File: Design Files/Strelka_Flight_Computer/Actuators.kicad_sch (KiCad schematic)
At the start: 10 parts, among them J3 DB125-3.5-4P-GN-S, J4 SM06B-GHS-TB(LF)(SN)

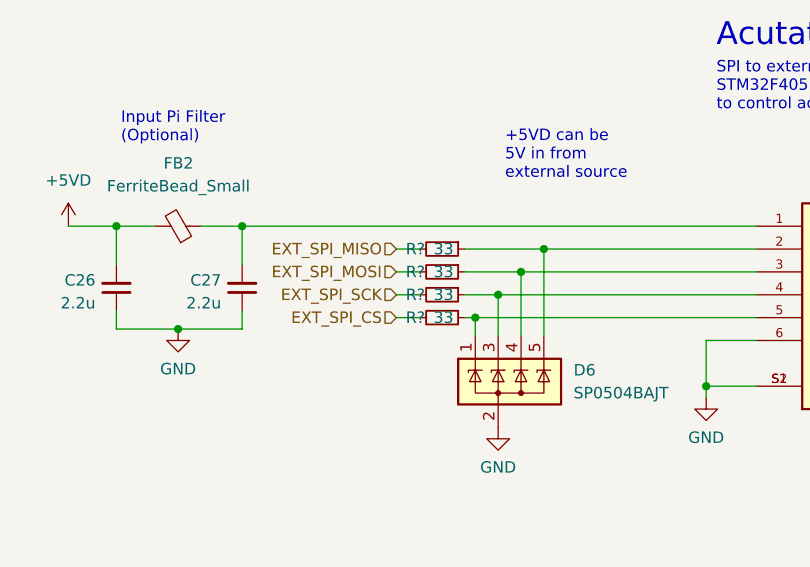
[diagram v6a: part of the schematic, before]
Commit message: Changed boost converter
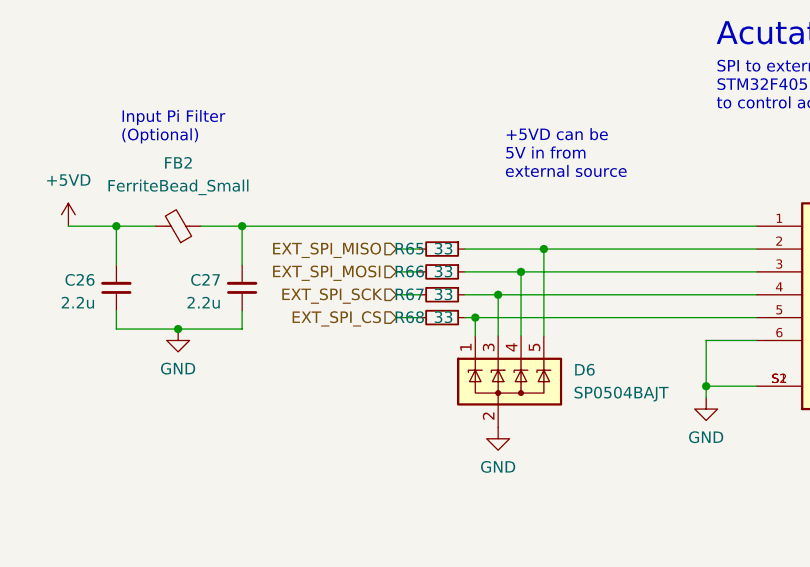
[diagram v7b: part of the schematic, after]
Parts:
- gave numbers to parts that had none: 4
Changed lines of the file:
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@@
   (symbol (lib_id "Device:R_Small") (at 191.135 90.17 270) (unit 1)
     (in_bom yes) (on_board yes)
-    (property "Reference" "R?" (id 0) (at 189.23 90.17 90)
+    (property "Reference" "R66" (id 0) (at 189.23 90.17 90)
       (effects (font (size 1.27 1.27)) (justify right))
     )
@@
   (symbol (lib_id "Device:R_Small") (at 191.135 95.25 270) (unit 1)
     (in_bom yes) (on_board yes)
-    (property "Reference" "R?" (id 0) (at 189.23 95.25 90)
+    (property "Reference" "R68" (id 0) (at 189.23 95.25 90)
       (effects (font (size 1.27 1.27)) (justify right))
     )
@@
   (symbol (lib_id "Device:R_Small") (at 191.135 92.71 270) (unit 1)
     (in_bom yes) (on_board yes)
-    (property "Reference" "R?" (id 0) (at 189.23 92.71 90)
+    (property "Reference" "R67" (id 0) (at 189.23 92.71 90)
       (effects (font (size 1.27 1.27)) (justify right))
     )
@@
   (symbol (lib_id "Device:R_Small") (at 191.135 87.63 270) (unit 1)
     (in_bom yes) (on_board yes)
-    (property "Reference" "R?" (id 0) (at 189.23 87.63 90)
+    (property "Reference" "R65" (id 0) (at 189.23 87.63 90)
       (effects (font (size 1.27 1.27)) (justify right))
     )

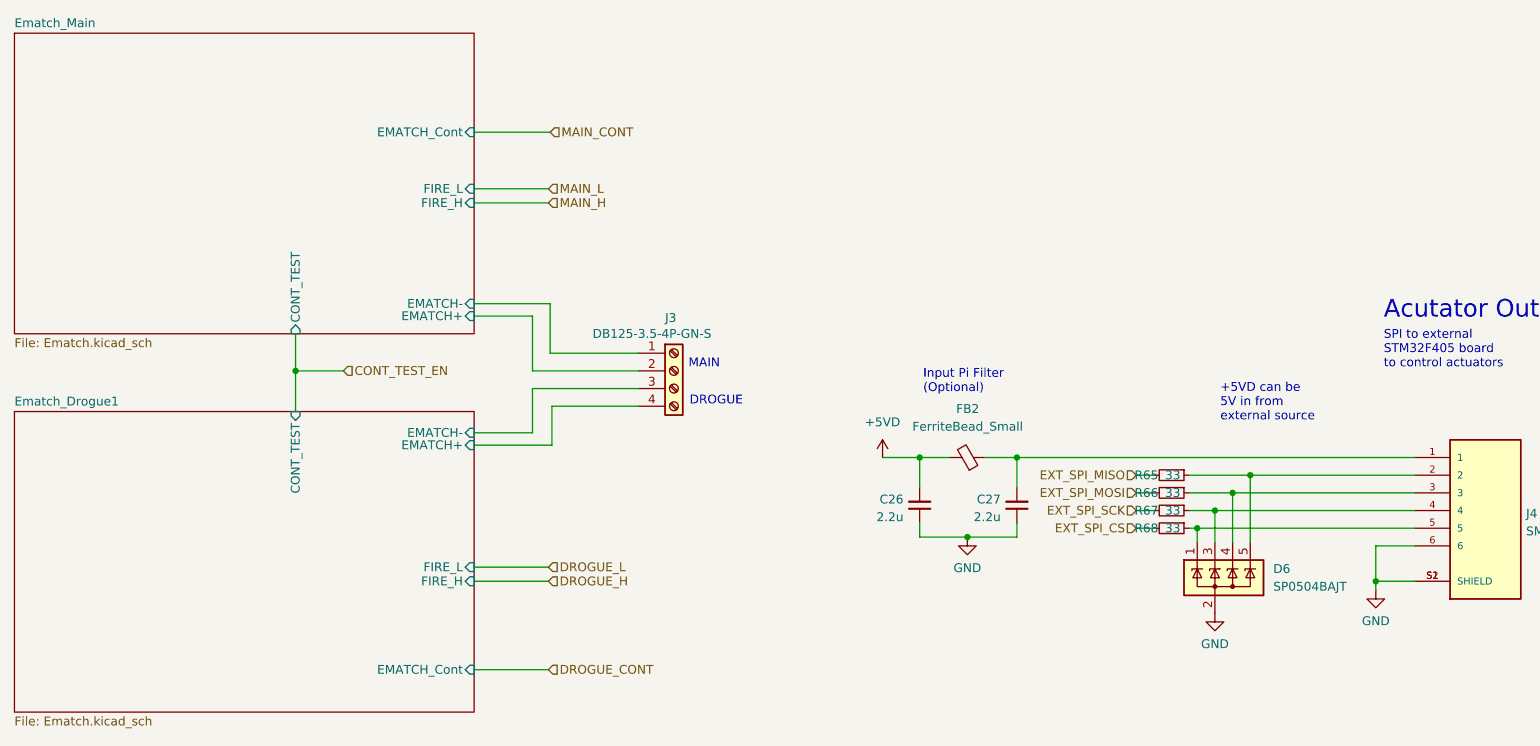
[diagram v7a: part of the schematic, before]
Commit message: Started component placement
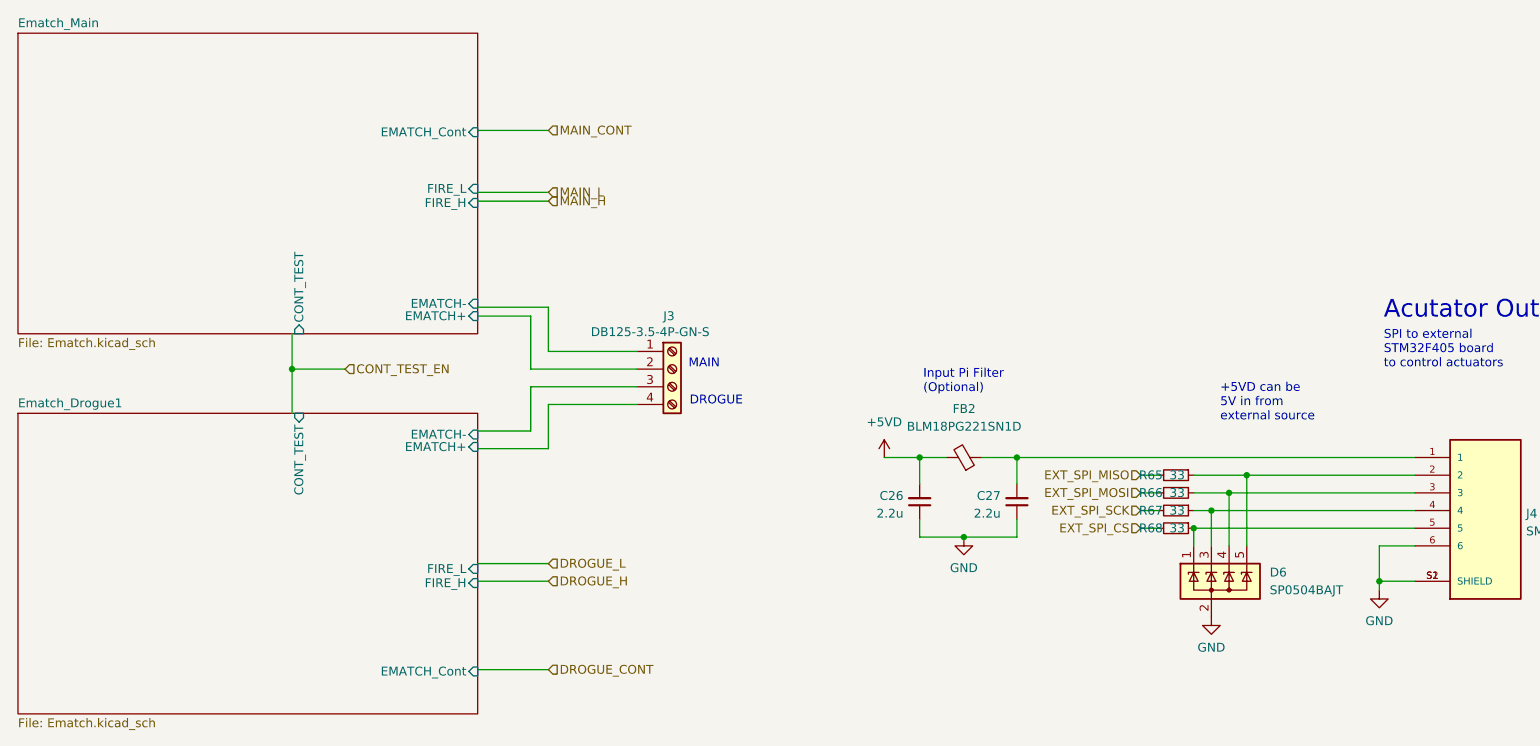
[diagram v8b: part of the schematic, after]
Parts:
- FB2: value FerriteBead_Small -> BLM18PG221SN1D; LCSC# (none) -> C80165
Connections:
- net Ematch_Drogue1/EMATCH+: no longer J3.4 (Pin_4)
- net Ematch_Drogue1/EMATCH-: no longer J3.3 (Pin_3)
- net Ematch_Main/EMATCH-: no longer J3.1 (Pin_1)
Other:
- moved on the sheet: C26, C27, D6, R65, R66, R67, R68
